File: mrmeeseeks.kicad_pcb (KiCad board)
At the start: 2 copper layers, 36 parts, among them U1 MCP23017

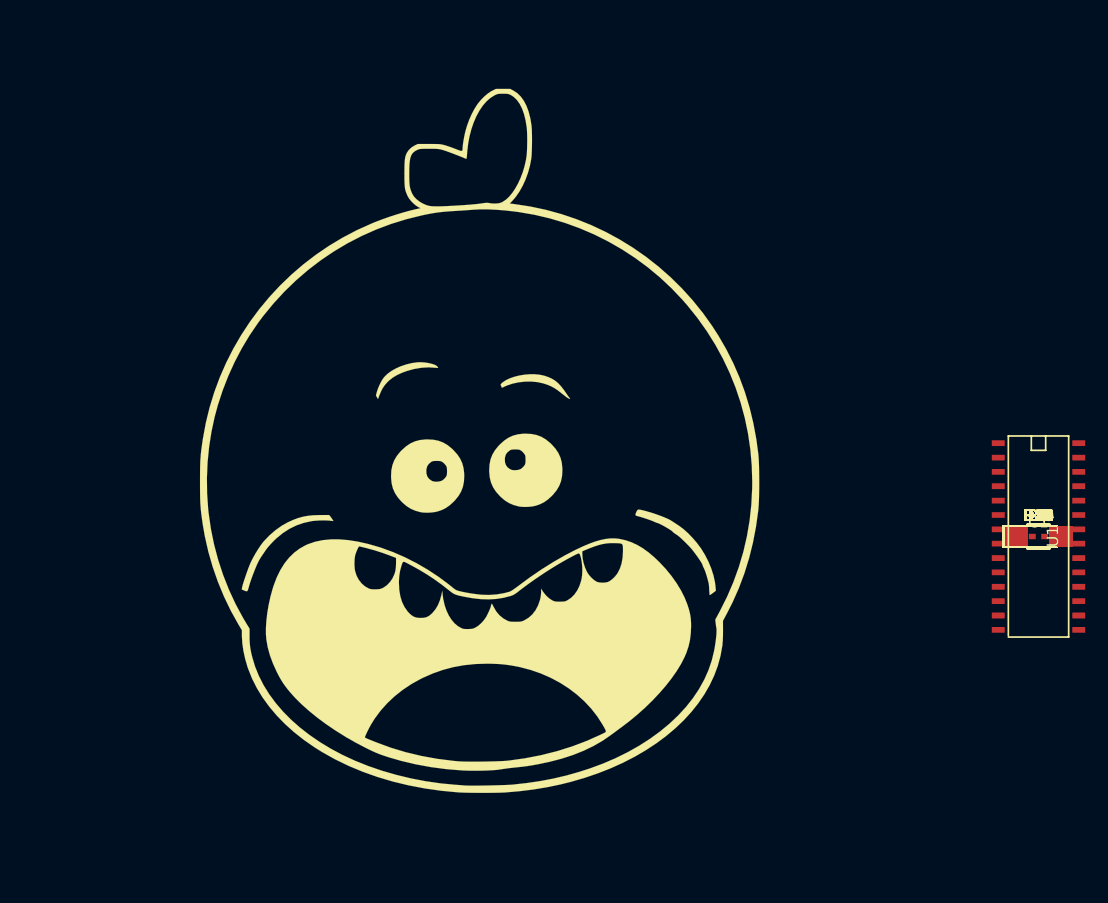
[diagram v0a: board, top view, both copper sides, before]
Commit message: Edge Cuts to PCB
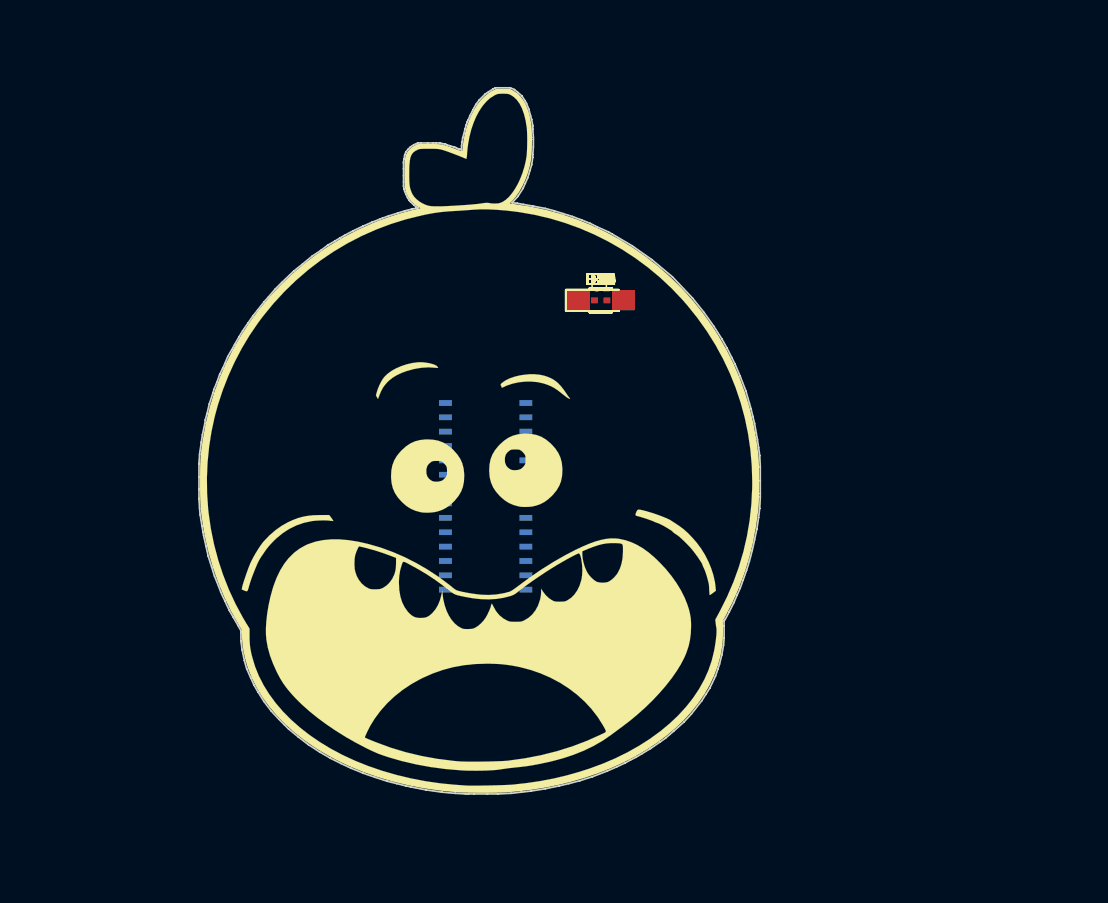
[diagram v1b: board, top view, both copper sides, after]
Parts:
- U1: moved to B.Cu
- moved U1 49.0 mm to (99.6, 101.4), turned to 90 degrees
- moved C1 44.0 mm to (109.8, 84.1)
- moved D1 44.0 mm to (109.8, 84.1)
- moved D10 44.0 mm to (109.8, 84.1)
- moved D11 44.0 mm to (109.8, 84.1)
- moved D12 44.0 mm to (109.8, 84.1)
- moved D13 44.0 mm to (109.8, 84.1)
- moved D14 44.0 mm to (109.8, 84.1)
- moved D15 44.0 mm to (109.8, 84.1)
- moved D16 44.0 mm to (109.8, 84.1)
- moved D2 44.0 mm to (109.8, 84.1)
- moved D3 44.0 mm to (109.8, 84.1)
- moved D4 44.0 mm to (109.8, 84.1)
- moved D5 44.0 mm to (109.8, 84.1)
- moved D6 44.0 mm to (109.8, 84.1)
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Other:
- board outline added: 49.6 x 62.4 mm

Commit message: Updated PCB Design
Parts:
- removed D10, D11, D12, D13, D14, D15, D16: LED, LEDs:LED_1206_HandSoldering
- removed R10, R11, R12, R13, R14, R15, R16: 220, Resistors_SMD:R_1206_HandSoldering
- added X1: Badgelife_shitty_connector, mrmeeseeks-addon:Badgelife-Shitty-2x2, F.Cu at (99.6, 122.5)
- C1: footprint Capacitors_SMD:C_0402_NoSilk -> mrmeeseeks-addon:C_0402_NoSilk_NoText; moved to B.Cu
- D1, D2, D3, D4, D5, D6, D7, D8, D9: footprint LEDs:LED_1206_HandSoldering -> mrmeeseeks-addon:LED_1206_HandSoldering_MinSilk
- R1, R2, R3, R4, R5, R6, R7, R8, R9: footprint Resistors_SMD:R_1206_HandSoldering -> mrmeeseeks-addon:R_1206_HandSoldering_NoSilk; moved to B.Cu
- moved D1 37.7 mm to (76.7, 102.1), turned to 275 degrees
- moved R1 37.7 mm to (76.7, 102.1), turned to 275 degrees
- moved D2 33.2 mm to (77.8, 93.1), turned to 250 degrees
- moved R2 33.2 mm to (77.8, 93.1), turned to 250 degrees
- moved D3 27.3 mm to (82.5, 85.2), turned to 228 degrees
- moved R3 27.3 mm to (82.5, 85.2), turned to 228 degrees
- moved C1 26.0 mm to (99.8, 108.2)
- moved D9 21.4 mm to (121.6, 102.0), turned to 85 degrees
- moved R9 21.4 mm to (121.6, 102.0), turned to 85 degrees
- moved D4 20.5 mm to (89.8, 79.9), turned to 205 degrees
- moved R4 20.5 mm to (89.8, 79.9), turned to 205 degrees
- moved D8 13.9 mm to (120.4, 93.0), turned to 110 degrees
- moved R8 13.9 mm to (120.4, 93.0), turned to 110 degrees
- moved D5 12.7 mm to (98.8, 77.9), turned to 180 degrees
- moved R5 12.7 mm to (98.8, 77.9), turned to 180 degrees
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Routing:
- added copper zone on B.Cu, net GND
- added copper zone on F.Cu, net GND

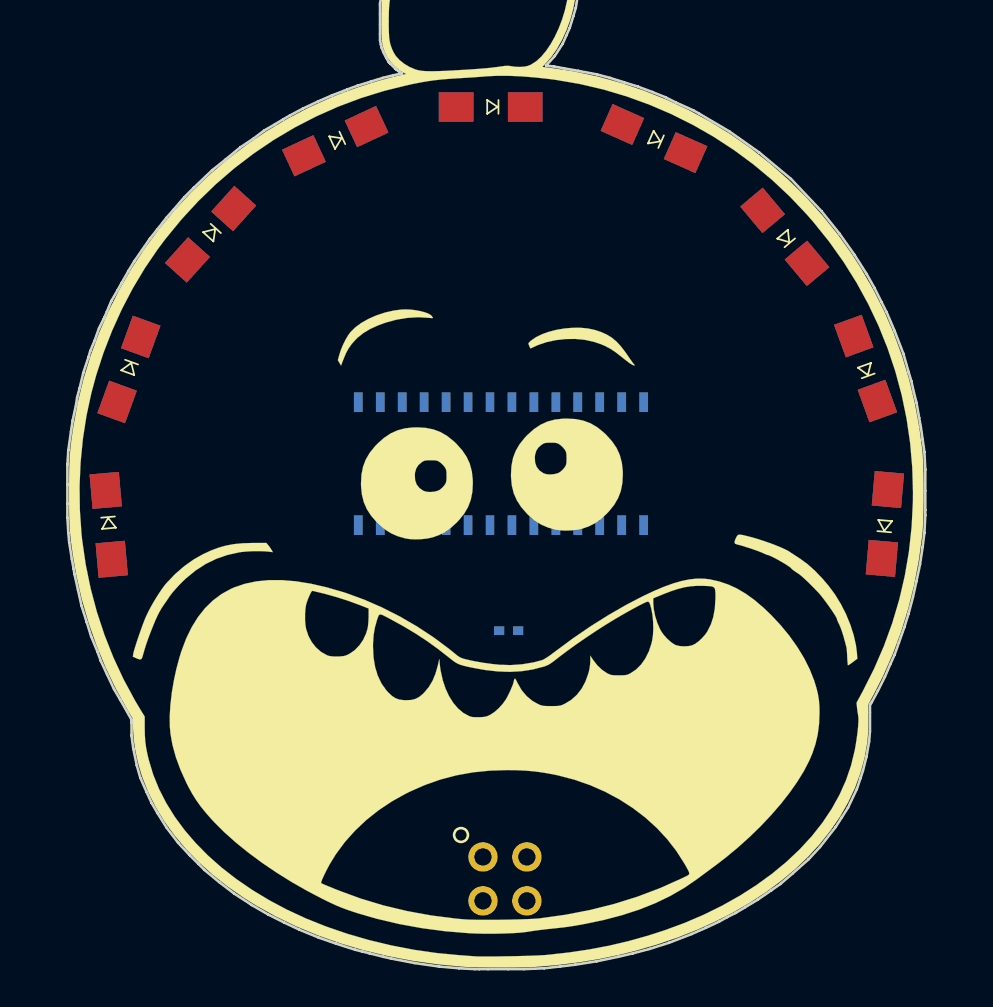
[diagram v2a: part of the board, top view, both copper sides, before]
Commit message: Draft 1 of PCB Done
All tracers added
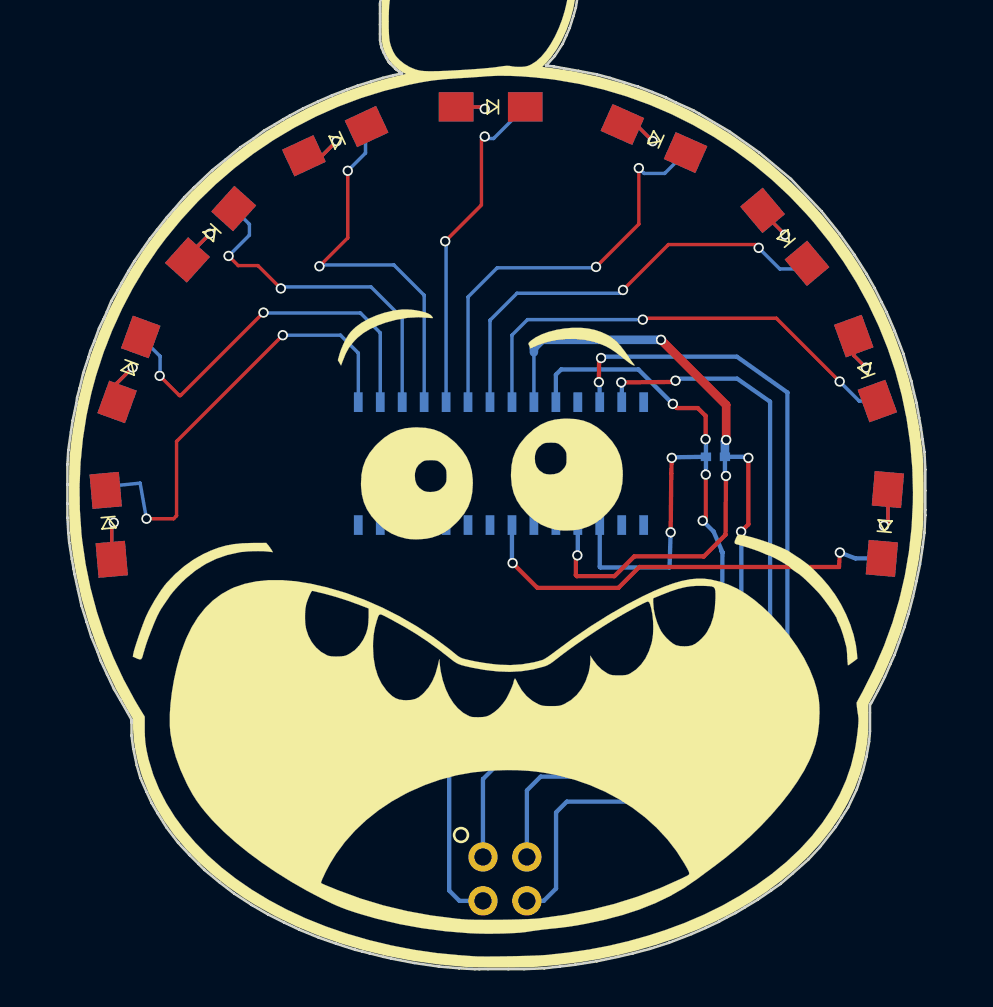
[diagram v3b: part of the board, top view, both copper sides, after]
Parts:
- moved C1 15.6 mm to (111.8, 98.1), turned to 180 degrees
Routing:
- net +3V3: track 0.00 -> 72.3 mm, vias 0 -> 6
- net GND: track 0.00 -> 68.8 mm, vias 0 -> 6
- net scl: track 0.00 -> 54.3 mm, vias 0 -> 2
- net sda: track 0.00 -> 47.4 mm, vias 0 -> 2
- net Net-(R8-Pad1): track 0.00 -> 27.4 mm, vias 0 -> 2
- net Net-(R1-Pad1): track 0.00 -> 26.6 mm, vias 0 -> 2
- net Net-(R7-Pad1): track 0.00 -> 25.6 mm, vias 0 -> 2
- net Net-(R9-Pad1): track 0.00 -> 25.5 mm, vias 0 -> 2
- net Net-(R6-Pad1): track 0.00 -> 24.3 mm, vias 0 -> 2
- net Net-(R2-Pad1): track 0.00 -> 22.4 mm, vias 0 -> 2
- net Net-(R4-Pad1): track 0.00 -> 22.2 mm, vias 0 -> 2
- net Net-(R3-Pad1): track 0.00 -> 20.1 mm, vias 0 -> 2
- net Net-(R5-Pad1): track 0.00 -> 19.5 mm, vias 0 -> 2
- net Net-(D2-Pad2): track 0.00 -> 4.73 mm, vias 0 -> 1
- net Net-(D4-Pad2): track 0.00 -> 4.48 mm, vias 0 -> 1
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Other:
- board text added: "ILLEGAL TO SELL ON EBAY"

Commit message: Design By Updates
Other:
- board text added: "Designed By: SparX MyndFyre"
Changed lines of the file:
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@@
     (area 74.194599 65.253799 123.976201 127.837001)
     (thickness 1.6)
-    (drawings 256)
+    (drawings 257)
     (tracks 253)
     (zones 0)
@@
     (visible_elements 7FFFFFFF)
     (pcbplotparams
-      (layerselection 0x00030_80000001)
-      (usegerberextensions false)
+      (layerselection 0x010fc_80000001)
+      (usegerberextensions true)
       (excludeedgelayer true)
       (linewidth 0.100000)
@@
       (plotinvisibletext false)
       (padsonsilk false)
-      (subtractmaskfromsilk false)
+      (subtractmaskfromsilk true)
       (outputformat 1)
       (mirror false)
-      (drillshape 1)
+      (drillshape 0)
       (scaleselection 1)
-      (outputdirectory ""))
+      (outputdirectory gerbers/))
   )
   (net 0 "")
@@
     )
   )
+  (gr_text "Designed By:\nSparX\nMyndFyre" (at 90.9701 116.586) (layer B.SilkS)
+    (effects (font (size 1 1) (thickness 0.0625)) (justify mirror))
+  )
   (gr_text "ILLEGAL TO SELL\nON EBAY" (at 98.9584 90.2462) (layer B.SilkS)

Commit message: Updates to Soldermask Layer
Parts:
- removed the G*** at (99.0, 96.5)
- added G***: LOGO, mrmeeseeks-addon-design:soldermask, F.Cu at (99.1, 96.5)

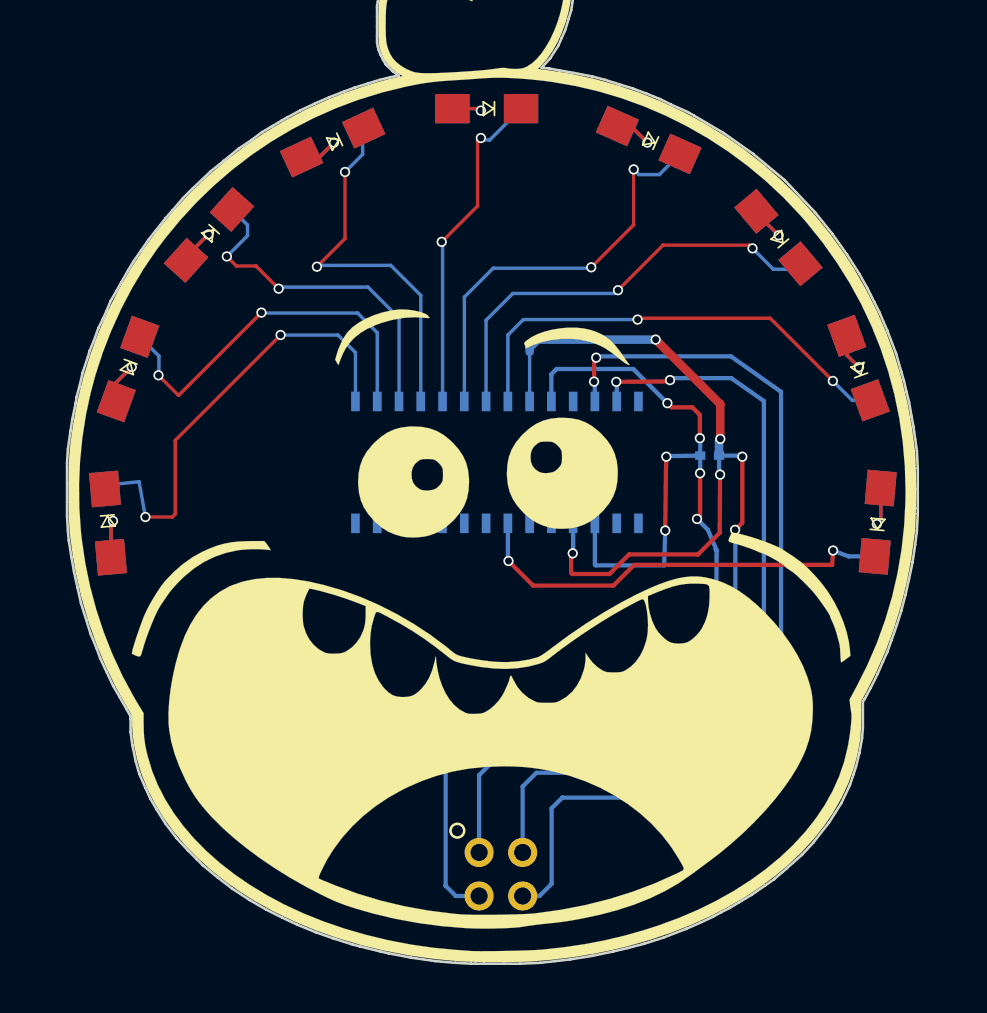
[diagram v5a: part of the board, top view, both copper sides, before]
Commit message: Draft 2
Redesigned tracers
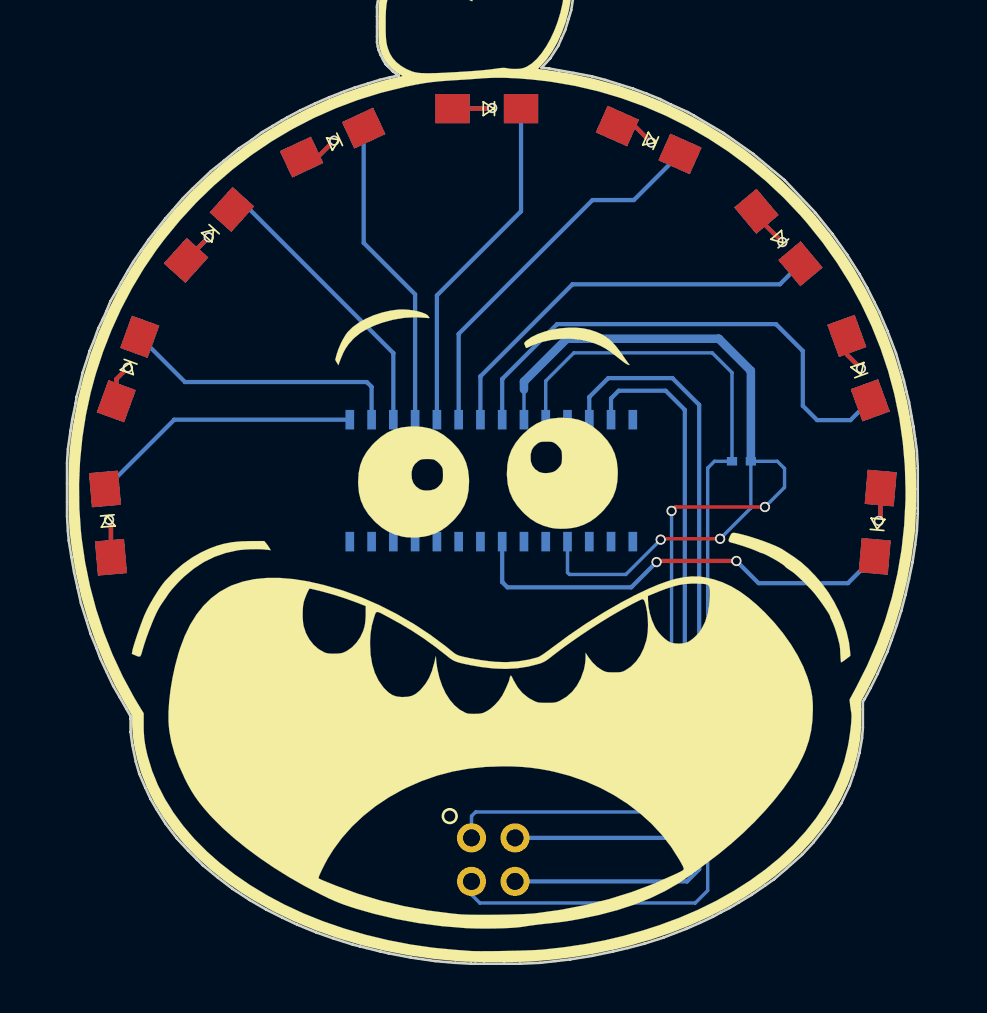
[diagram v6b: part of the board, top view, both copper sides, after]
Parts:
- moved C1 1.88 mm to (113.6, 98.5)
- moved U1 1.12 mm to (99.0, 99.6)
- moved X1 0.96 mm to (99.1, 121.7)
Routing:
- net Net-(R1-Pad1): track 26.6 -> 16.0 mm, vias 2 -> 0
- net GND: track 68.8 -> 60.7 mm, vias 6 -> 0
- net +3V3: track 72.3 -> 79.9 mm, vias 6 -> 4
- net scl: track 54.3 -> 47.0 mm, vias 2 -> 0
- net sda: track 47.4 -> 40.4 mm, vias 2 -> 0
- net Net-(R2-Pad1): track 22.4 -> 16.7 mm, vias 2 -> 0
- net Net-(R4-Pad1): track 22.2 -> 18.3 mm, vias 2 -> 0
- net Net-(R3-Pad1): track 20.1 -> 16.8 mm, vias 2 -> 0
- net Net-(R8-Pad1): track 27.4 -> 29.8 mm, vias 2 -> 0
- net Net-(R6-Pad1): track 24.3 -> 22.3 mm, vias 2 -> 0
- net Net-(R7-Pad1): track 25.6 -> 23.9 mm, vias 2 -> 0
- net Net-(D5-Pad2): track 3.41 -> 4.67 mm
- net Net-(D7-Pad2): track 3.89 -> 4.85 mm
- net Net-(R5-Pad1): track 19.5 -> 20.2 mm, vias 2 -> 0
- net Net-(R9-Pad1): track 25.5 -> 26.0 mm
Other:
- board text added: "#badgelife"
- board text added: "Designed By: MyndFyre SparX"
- board text added: "Thanks to: AND!XOR"
- board text removed: "Designed By: SparX MyndFyre"

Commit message: Updated Traces
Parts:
- U1: footprint SMD_Packages:SOIC-28 -> Libraries:SOIC-28_NoSilk
- moved C1 1.76 mm to (115.3, 99.1)
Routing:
- net GND: track 60.7 -> 90.4 mm
- net Net-(R5-Pad1): track 20.2 -> 38.7 mm
- net +3V3: track 79.9 -> 95.7 mm, vias 4 -> 2
- net Net-(R4-Pad1): track 18.3 -> 30.5 mm
- net Net-(R1-Pad1): track 16.0 -> 23.0 mm
- net sda: track 40.4 -> 46.9 mm
- net Net-(R3-Pad1): track 16.8 -> 22.4 mm
- net scl: track 47.0 -> 52.4 mm
- net Net-(R8-Pad1): track 29.8 -> 33.9 mm
- net Net-(R7-Pad1): track 23.9 -> 25.6 mm
- net Net-(R9-Pad1): track 26.0 -> 27.6 mm
- net Net-(R6-Pad1): track 22.3 -> 23.8 mm
- net Net-(D5-Pad2): track 4.67 -> 3.96 mm
- net Net-(D7-Pad2): track 4.85 -> 4.23 mm
- net Net-(R2-Pad1): track 16.7 -> 17.3 mm
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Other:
- board text added: "Mr. Meeseeks"
